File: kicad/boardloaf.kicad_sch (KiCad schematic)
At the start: 41 parts, among them J1 AudioJack4, J2 AudioJack4, SW1 SW_Push, SW10 SW_Push, SW11 SW_Push, SW12 SW_Push, SW13 SW_Push, SW14 SW_Push, SW15 SW_Push, SW16 SW_Push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

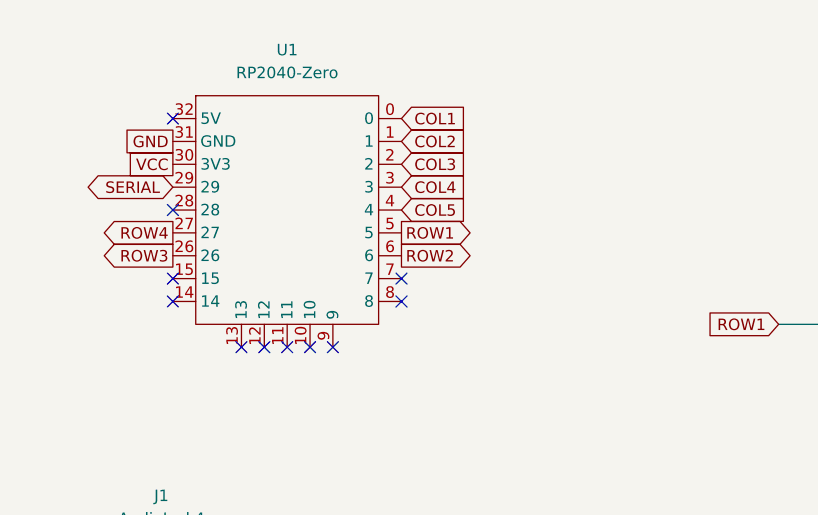
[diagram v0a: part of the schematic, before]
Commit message: fix schema and add jumper
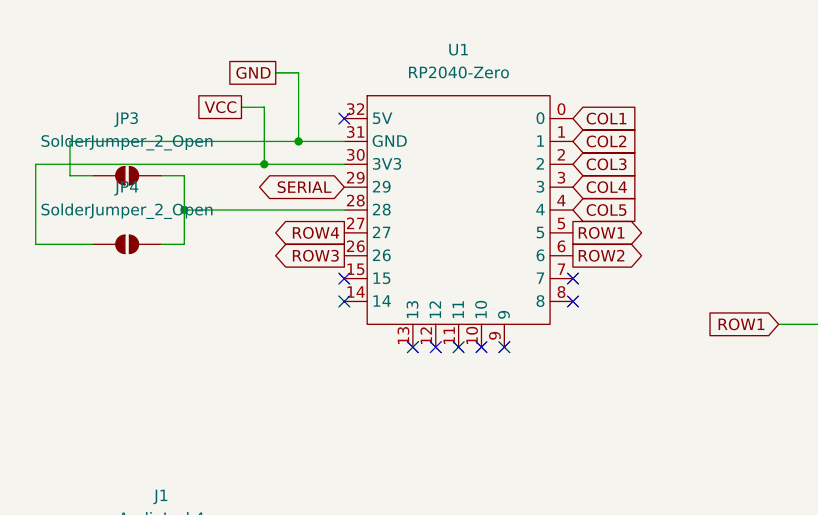
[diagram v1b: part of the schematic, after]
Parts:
- added JP3, JP4: SolderJumper_2_Open, symbol Jumper:SolderJumper_2_Open
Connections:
- net GND: now also JP3.1 (A)
- net VCC: now also JP4.1 (A)
- net at U1.28: now also JP3.2 (B), JP4.2 (B)
- no-connect marks 11 -> 10
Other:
- moved on the sheet: U1
